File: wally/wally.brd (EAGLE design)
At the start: 5 x 8.6 mm, 34 parts, among them IC1 ESP32-S3-WROOM-1-N4, IC2 XTLV61048DBVR, IC3 TLV1117LV33DCYR, J6 USBC, U1 RA-01H

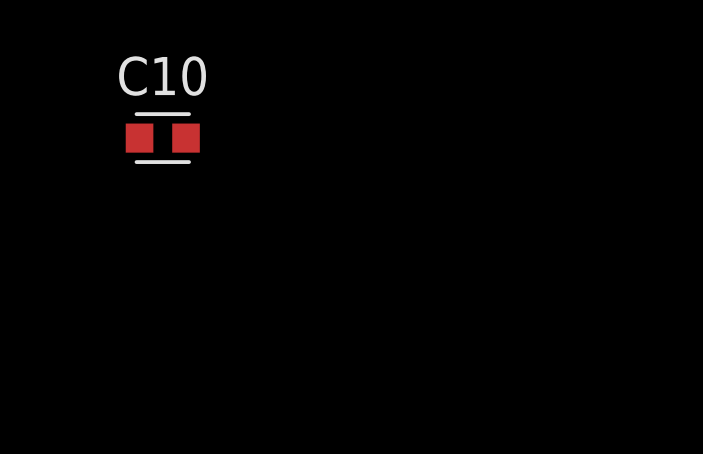
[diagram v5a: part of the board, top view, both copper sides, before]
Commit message: add ds3231 rtc
treat as 5 pin header
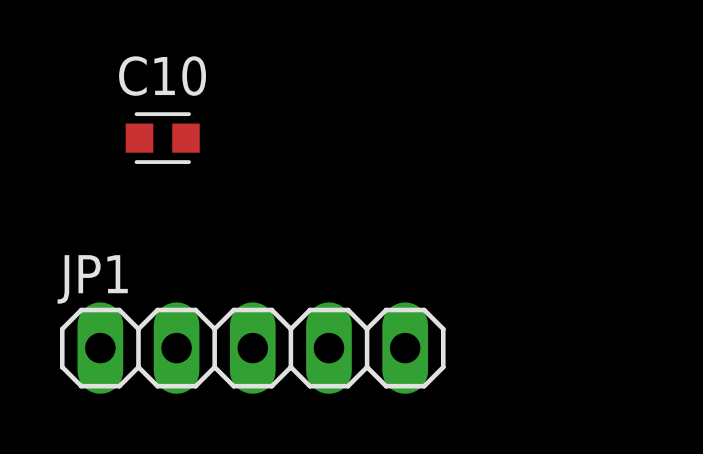
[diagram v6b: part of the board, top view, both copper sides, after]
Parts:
- added JP1: (no value), pinhead:1X05
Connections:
- new net SDA0: JP1.4
- new net SDA1: JP1.3
- net 3V3: now also JP1.5
- net GND: now also JP1.1
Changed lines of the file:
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@@
 <attribute name="VOLTAGE_RATING" value="" x="-91" y="-125" size="1.778" layer="27" font="vector" ratio="15" display="off"/>
+</element>
+<element name="JP1" library="pinhead" library_urn="urn:adsk.eagle:library:325" package="1X05" package3d_urn="urn:adsk.eagle:package:22469/2" value="" x="-88" y="-132" smashed="yes">
+<attribute name="NAME" x="-94.4262" y="-130.1712" size="1.27" layer="25" ratio="10"/>
+<attribute name="POPULARITY" value="69" x="-88" y="-132" size="1.778" layer="27" font="vector" ratio="15" display="off"/>
+<attribute name="VALUE" x="-94.35" y="-135.175" size="1.27" layer="27"/>
 </element>
 </elements>
@@
 <contactref element="C8" pad="2"/>
 <contactref element="C10" pad="2"/>
+<contactref element="JP1" pad="1"/>
+<wire x1="-90.2254" y1="-125" x2="-93.08" y2="-132" width="0" layer="19" extent="1-1"/>
 <wire x1="-90.2254" y1="-118" x2="-90.2254" y2="-125" width="0" layer="19" extent="1-1"/>
 <wire x1="-90.2254" y1="-111" x2="-90.2254" y2="-118" width="0" layer="19" extent="1-1"/>
@@
 <wire x1="-33.7746" y1="-67" x2="-38.7746" y2="-67" width="0" layer="19" extent="1-1"/>
 <wire x1="-51" y1="-57" x2="-43.7746" y2="-67" width="0" layer="19" extent="1-1"/>
-<wire x1="-16.66" y1="-45.225" x2="-33.7746" y2="-67" width="0" layer="19" extent="1-1"/>
-<wire x1="-16.66" y1="-38.775" x2="-16.66" y2="-45.225" width="0" layer="19" extent="1-1"/>
 <wire x1="-50.7746" y1="-33" x2="-51" y2="-57" width="0" layer="19" extent="1-1"/>
 <wire x1="-49.1848" y1="-26" x2="-50.7746" y2="-33" width="0" layer="19" extent="1-1"/>
@@
 <wire x1="-40.7746" y1="-26" x2="-44.1848" y2="-26" width="0" layer="19" extent="1-1"/>
 <wire x1="-39.1848" y1="-16" x2="-40.7746" y2="-26" width="0" layer="19" extent="1-1"/>
-<wire x1="6" y1="-44.2254" x2="-16.66" y2="-38.775" width="0" layer="19" extent="1-1"/>
-<wire x1="8.05" y1="-42.75" x2="6" y2="-44.2254" width="0" layer="19" extent="1-1"/>
+<wire x1="-16.66" y1="-38.775" x2="-40.7746" y2="-26" width="0" layer="19" extent="1-1"/>
+<wire x1="-16.66" y1="-45.225" x2="-16.66" y2="-38.775" width="0" layer="19" extent="1-1"/>
+<wire x1="3" y1="-28.12" x2="-16.66" y2="-38.775" width="0" layer="19" extent="1-1"/>
+<wire x1="3" y1="-15.42" x2="3" y2="-28.12" width="0" layer="19" extent="1-1"/>
+<wire x1="8.05" y1="-42.75" x2="3" y2="-28.12" width="0" layer="19" extent="1-1"/>
+<wire x1="6" y1="-44.2254" x2="8.05" y2="-42.75" width="0" layer="19" extent="1-1"/>
 <wire x1="9" y1="-45.25" x2="8.05" y2="-42.75" width="0" layer="19" extent="1-1"/>
 <wire x1="12" y1="-46.8152" x2="9" y2="-45.25" width="0" layer="19" extent="1-1"/>
@@
 <wire x1="9.49" y1="-75.75" x2="15.81" y2="-69.9" width="0" layer="19" extent="1-1"/>
 <wire x1="15" y1="-81.3179" x2="9.49" y2="-75.75" width="0" layer="19" extent="1-1"/>
-<wire x1="3" y1="-28.12" x2="8.05" y2="-42.75" width="0" layer="19" extent="1-1"/>
-<wire x1="3" y1="-15.42" x2="3" y2="-28.12" width="0" layer="19" extent="1-1"/>
 <wire x1="17" y1="-96.6821" x2="15" y2="-81.3179" width="0" layer="19" extent="1-1"/>
 <wire x1="3" y1="-96.6821" x2="17" y2="-96.6821" width="0" layer="19" extent="1-1"/>
@@
 <contactref element="IC3" pad="2"/>
 <contactref element="C10" pad="1"/>
+<contactref element="JP1" pad="5"/>
+<wire x1="-82.92" y1="-132" x2="-91.7746" y2="-125" width="0" layer="19" extent="1-1"/>
 <wire x1="-90.15" y1="-104" x2="-91.7746" y2="-125" width="0" layer="19" extent="1-1"/>
 <wire x1="-83.85" y1="-104" x2="-90.15" y2="-104" width="0" layer="19" extent="1-1"/>
@@
 <contactref element="IC2" pad="3"/>
 </signal>
+<signal name="SDA0">
+<contactref element="JP1" pad="4"/>
+</signal>
+<signal name="SDA1">
+<contactref element="JP1" pad="3"/>
+</signal>
 </signals>

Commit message: reset switch
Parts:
- added C11, C13, C16: 100n, Capacitor:CAPC1608X85
- added C12: 22u, Capacitor:CAPC1608X85
- added R1: 10k, Resistor:RESC1608X60
- added R4: 1k, Resistor:RESC1608X60
- added S1: TS-1187A-B-A-B, SamacSys_Parts:TS1187ABAB
- moved J6 72.2 mm to (32.0, -95.0)
- moved JP1 48.7 mm to (-40.0, -124.0), turned to 90 degrees
- moved IC1 23.1 mm to (13.0, -90.0)
- moved U1 20.1 mm to (8.00, -69.0), turned to 90 degrees
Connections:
- removed net USB_D+: J6.A6, J6.B6
- removed net USB_D-: J6.A7, J6.B7
- new net EN: R4.2
- new net N$1: C13.1, IC1.3, R1.2
- new net N$4: C16.2, R4.1, S1.A1, S1.B1
- new net USB_N: IC1.13, J6.A7, J6.B7
- new net USB_P: IC1.14, J6.A6, J6.B6
- net 3V3: now also C11.1, C12.1, R1.1
- net GND: now also C11.2, C12.2, C13.2, C16.1, S1.C1, S1.D1

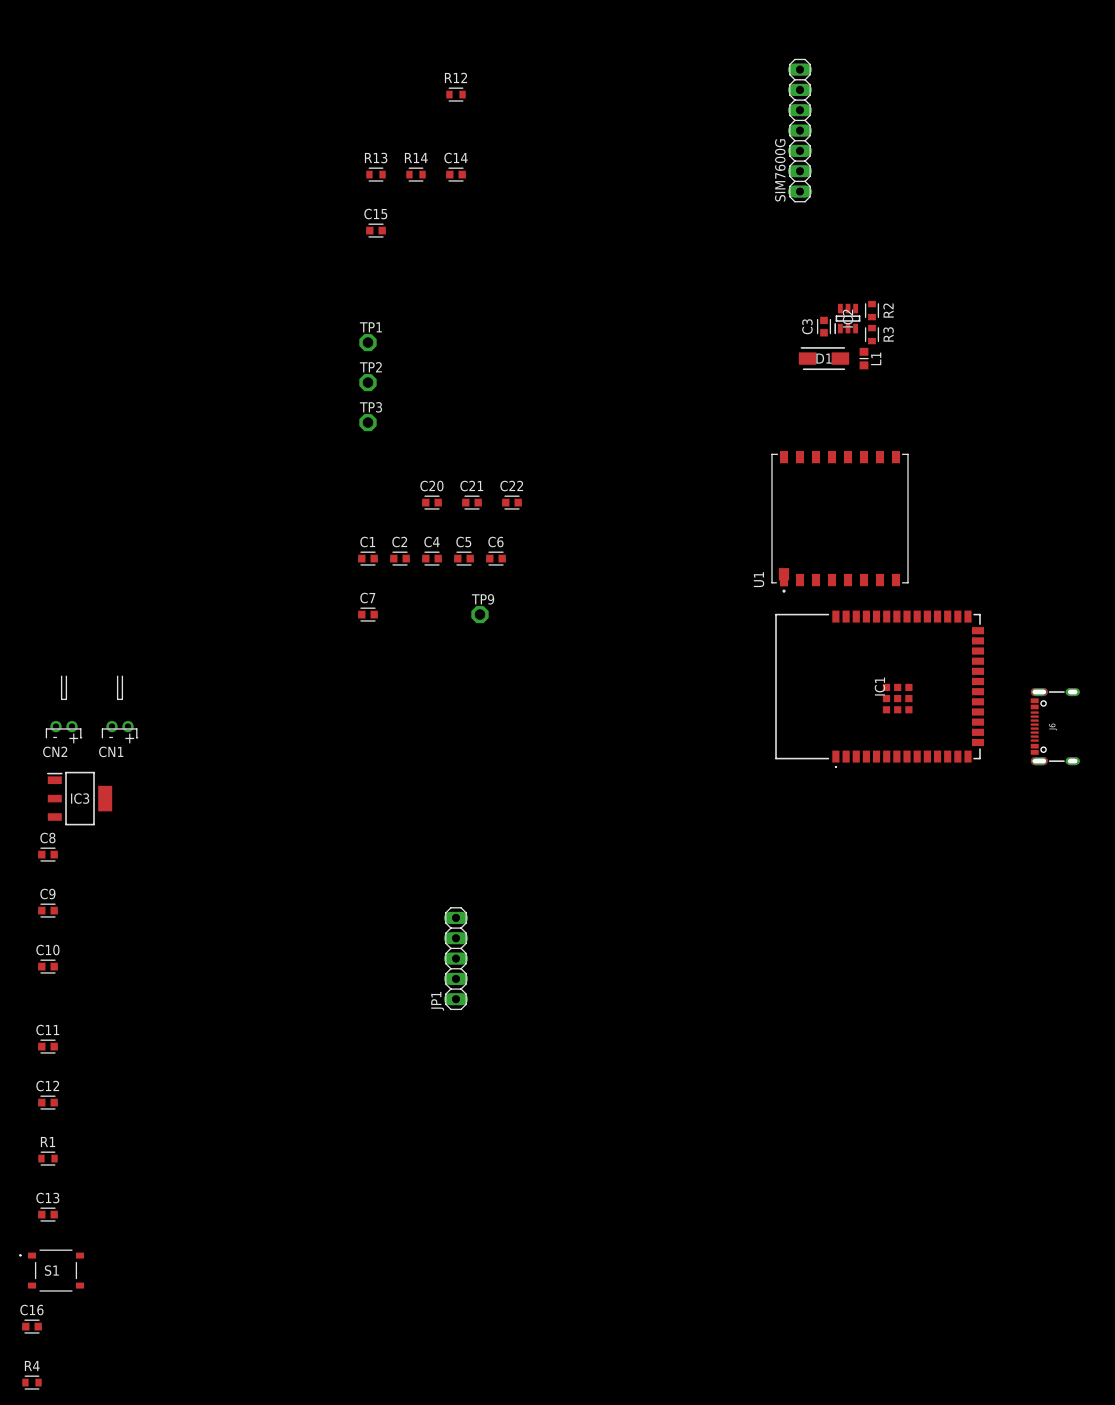
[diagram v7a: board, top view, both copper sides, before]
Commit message: switch to smaller esp
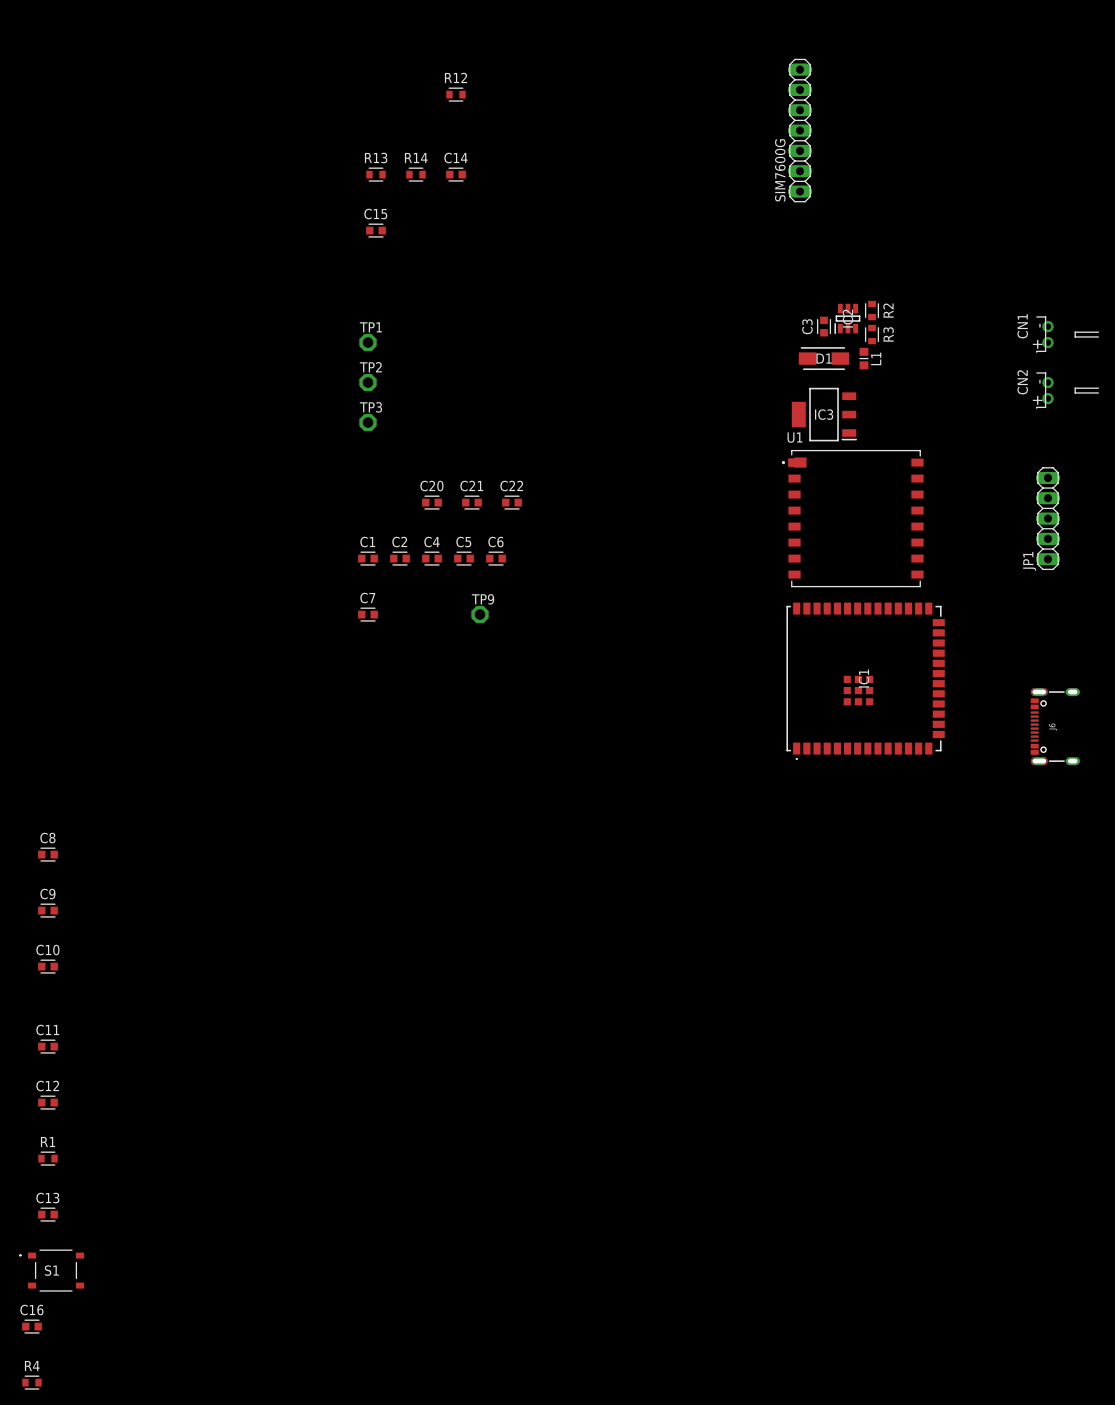
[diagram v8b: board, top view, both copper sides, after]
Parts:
- IC1: value ESP32-S3-WROOM-1-N4 -> ESP32-S3-WROOM-1U-N16; device SamacSys_Parts:ESP32S3WROOM1N4 -> SamacSys_Parts:ESP32S3WROOM1UN16
- moved CN2 130.0 mm to (34.0, -53.0), turned to 270 degrees
- moved CN1 125.9 mm to (34.0, -46.0), turned to 270 degrees
- moved IC3 104.7 mm to (6.00, -56.0), turned to 180 degrees
- moved JP1 92.2 mm to (34.0, -69.0)
- moved IC1 2.24 mm to (11.0, -89.0)
- moved U1 2.00 mm to (10.0, -69.0), turned to 0 degrees
